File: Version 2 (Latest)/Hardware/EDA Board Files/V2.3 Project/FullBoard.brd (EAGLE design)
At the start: 281.5 x 99 mm, 187 parts, among them IC1 LM3914V, IC2 SGTL5000XNAA3, IC4 MCP73113-16SI_MF, IC5 NCP163ASN330T1G, J1 SJ-3524-SMT-TR, J10 SJ-3524-SMT-TR, J2 Teensy2, J3 Teensy1, J4 SJ-3524-SMT-TR, J7 1981584-1, J9 SJ-3524-SMT-TR, Q2 DMG9926USD-13, SW1 GATERON_LOW_PROFILE, SW10 GATERON_LOW_PROFILE, SW11 GATERON_LOW_PROFILE, SW12 GATERON_LOW_PROFILE, SW13 GATERON_LOW_PROFILE, SW14 GATERON_LOW_PROFILE, SW15 GATERON_LOW_PROFILE, SW16 GATERON_LOW_PROFILE, SW17 GATERON_LOW_PROFILE, SW18 GATERON_LOW_PROFILE, SW19 GATERON_LOW_PROFILE, SW2 GATERON_LOW_PROFILE, SW20 GATERON_LOW_PROFILE, SW21 GATERON_LOW_PROFILE, SW22 GATERON_LOW_PROFILE, SW23 GATERON_LOW_PROFILE, SW24 GATERON_LOW_PROFILE, SW25 GATERON_LOW_PROFILE, SW26 GATERON_LOW_PROFILE, SW27 GATERON_LOW_PROFILE, SW28 GATERON_LOW_PROFILE, SW29 GATERON_LOW_PROFILE, SW3 GATERON_LOW_PROFILE, SW30 GATERON_LOW_PROFILE, SW31 GATERON_LOW_PROFILE, SW32 GATERON_LOW_PROFILE, SW33 GATERON_LOW_PROFILE, SW34 GATERON_LOW_PROFILE, SW35 GATERON_LOW_PROFILE, SW36 GATERON_LOW_PROFILE, SW37 GATERON_LOW_PROFILE, SW38 GATERON_LOW_PROFILE, SW39 GATERON_LOW_PROFILE, SW4 GATERON_LOW_PROFILE, SW40 GATERON_LOW_PROFILE, SW41 GATERON_LOW_PROFILE, SW42 GATERON_LOW_PROFILE, SW43 GATERON_LOW_PROFILE, SW44 GATERON_LOW_PROFILE, SW45 GATERON_LOW_PROFILE, SW46 GATERON_LOW_PROFILE, SW47 GATERON_LOW_PROFILE, SW5 GATERON_LOW_PROFILE, SW6 GATERON_LOW_PROFILE, SW7 GATERON_LOW_PROFILE, SW8 GATERON_LOW_PROFILE, SW9 GATERON_LOW_PROFILE, U1 W25Q128FVSIG, U2 ATMEGA4809-AFR, U3 PAM2401, U4 MAX6775XKA+21-0076E_MXM-M, U5 AP7313-15SAG-7SOT-23_DIO-L, U6 S25FL512SAGMFIR13SO3016_SPA-M

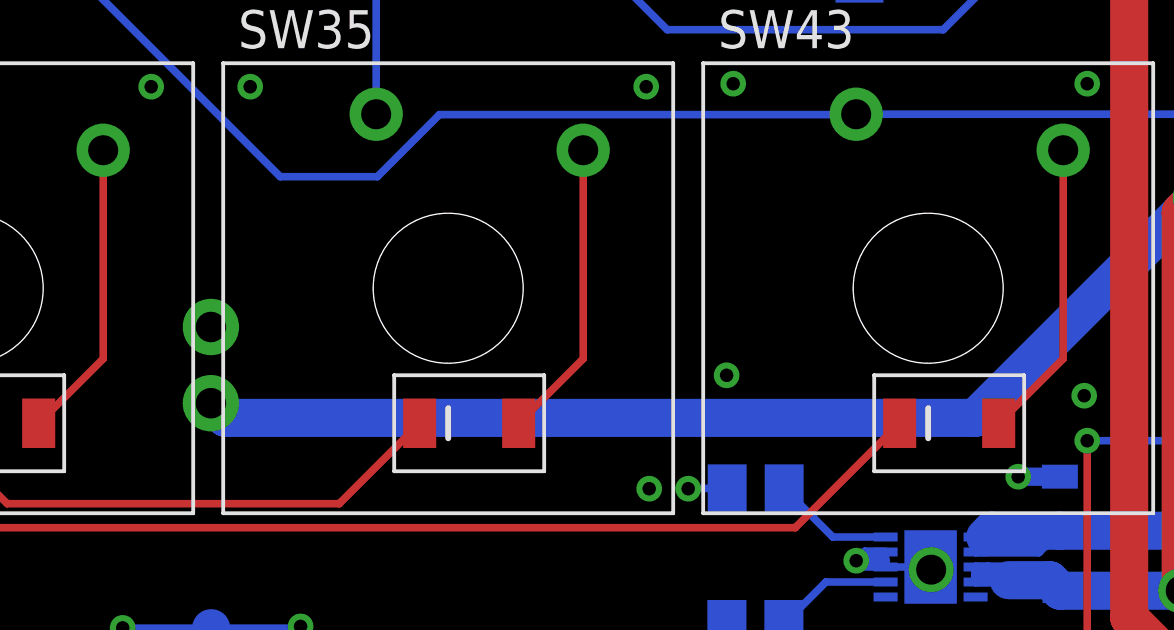
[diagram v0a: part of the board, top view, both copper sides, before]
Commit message: Updated battery connector on PCB
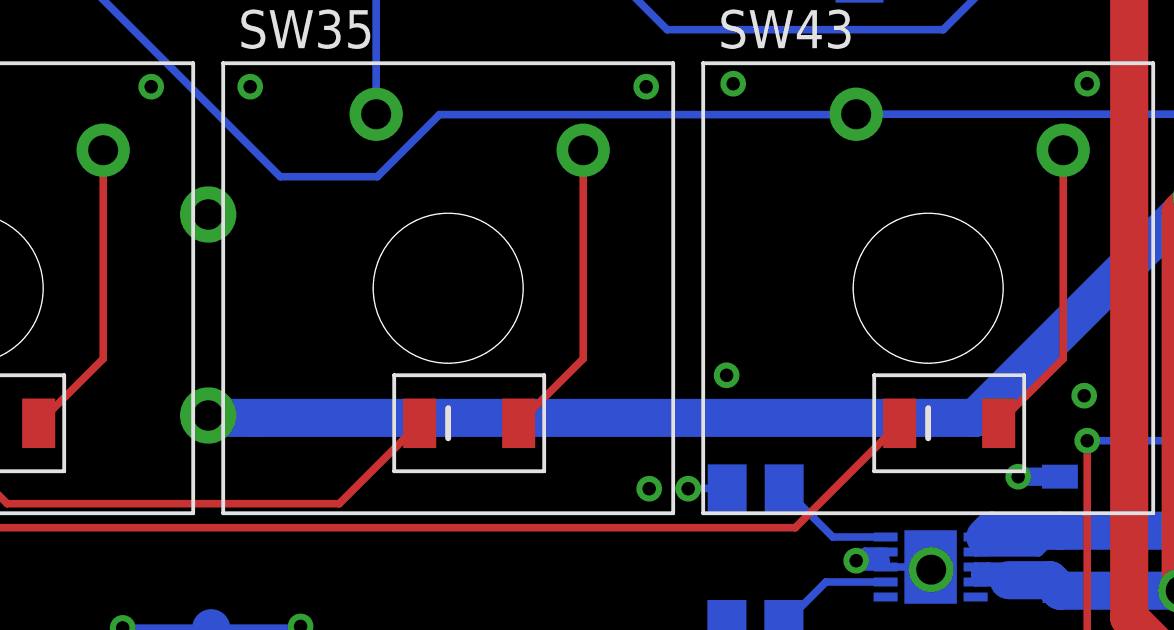
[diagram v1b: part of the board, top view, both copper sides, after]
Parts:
- removed J6: (no value), SparkFun-Connectors:1X02
- added J11, J12: (no value), SparkFun-Connectors:1X01
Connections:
- net GND: now also J12.1; no longer J6.2
- net LIPO+: now also J11.1; no longer J6.1
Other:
- board text added: "-"
- board text added: "Attach LiPo"
- board text added: "Here"
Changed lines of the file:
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@@
 <wire x1="3.59" y1="86.16" x2="3.59" y2="86.18" width="0.254" layer="26"/>
 <text x="168.01" y="46.07" size="1.4224" layer="26" rot="MR270">SI4703 Breakout</text>
+<text x="231.8" y="18.8" size="0.8128" layer="26" rot="MR0">Attach LiPo</text>
+<text x="230.2" y="17.8" size="0.8128" layer="26" rot="MR0">Here</text>
+<wire x1="229" y1="20.4" x2="229.6" y2="19.8" width="0.1524" layer="26"/>
+<wire x1="229" y1="20.4" x2="228.4" y2="19.8" width="0.1524" layer="26"/>
+<wire x1="229.6" y1="17.6" x2="229" y2="17" width="0.1524" layer="26"/>
+<wire x1="229" y1="17" x2="228.4" y2="17.6" width="0.1524" layer="26"/>
+<text x="229.7" y="12.2" size="1.778" layer="26" rot="MR0">+</text>
+<text x="229.54" y="23.39" size="2.1844" layer="26" rot="MR0">-</text>
 </plain>
 <attributes>
@@
 <attribute name="VALUE" x="270.83" y="73.21" size="1.27" layer="27" rot="R180" align="center"/>
 </element>
-<element name="J6" library="SparkFun-Connectors" package="1X02" value="" x="229.09" y="15.75" smashed="yes" rot="MR90">
-<attribute name="NAME" x="230.487" y="14.48" size="0.6096" layer="26" font="vector" ratio="20" rot="MR90"/>
-<attribute name="VALUE" x="227.058" y="14.48" size="0.6096" layer="28" font="vector" ratio="20" rot="MR90"/>
-</element>
 <element name="J7" library="audio amplifier example" library_urn="urn:adsk.eagle:library:970892" package="1981584-1" package3d_urn="urn:adsk.eagle:package:970926/2" value="1981584-1" x="281.03" y="9.68" smashed="yes" rot="MR270">
 <attribute name="MFPN" value="" x="434.7" y="-122.4" size="1.778" layer="28" rot="MR270" display="off"/>
@@
 <element name="TP3" library="SparkFun-Connectors" library_urn="urn:adsk.eagle:library:513" package="PAD.03X.05" package3d_urn="urn:adsk.eagle:package:38285/1" value="TEST-POINT3X5" x="273.23" y="46.23" smashed="yes" rot="MR0"/>
 <element name="TP4" library="SparkFun-Connectors" library_urn="urn:adsk.eagle:library:513" package="PAD.03X.05" package3d_urn="urn:adsk.eagle:package:38285/1" value="TEST-POINT3X5" x="229.1" y="8.25" smashed="yes" rot="MR0"/>
+<element name="J11" library="SparkFun-Connectors" library_urn="urn:adsk.eagle:library:513" package="1X01" package3d_urn="urn:adsk.eagle:package:38028/1" value="" x="229" y="15.34" smashed="yes" rot="MR0">
+<attribute name="VALUE" x="230.27" y="13.816" size="0.6096" layer="28" font="vector" ratio="20" rot="MR0" align="top-left"/>
+</element>
+<element name="J12" library="SparkFun-Connectors" library_urn="urn:adsk.eagle:library:513" package="1X01" package3d_urn="urn:adsk.eagle:package:38028/1" value="" x="229" y="22.04" smashed="yes" rot="MR0">
+<attribute name="VALUE" x="230.27" y="20.516" size="0.6096" layer="28" font="vector" ratio="20" rot="MR0" align="top-left"/>
+</element>
 </elements>
 <signals>
@@
 <contactref element="U4" pad="2"/>
 <contactref element="R23" pad="2"/>
-<contactref element="J6" pad="2"/>
 <contactref element="Q2" pad="3"/>
 <contactref element="R24" pad="2"/>
@@
 <wire x1="229.1" y1="8.25" x2="226.16" y2="8.25" width="0.254" layer="16"/>
 <wire x1="226.16" y1="8.25" x2="226.15" y2="8.26" width="0.254" layer="16"/>
+<contactref element="J12" pad="1"/>
 </signal>
 <signal name="SCL">
@@
 </signal>
 <signal name="LIPO+">
-<contactref element="J6" pad="1"/>
 <contactref element="U$1" pad="P$2"/>
 <contactref element="U$1" pad="P$5"/>
@@
 <wire x1="265.27" y1="23.75" x2="263.05" y2="23.75" width="1.27" layer="16"/>
 <wire x1="263.05" y1="23.75" x2="261.9" y2="22.6" width="1.27" layer="16"/>
-<wire x1="254.56" y1="15.26" x2="229.58" y2="15.26" width="1.27" layer="16"/>
-<wire x1="229.09" y1="15.75" x2="229.58" y2="15.26" width="1.27" layer="16"/>
+<wire x1="254.56" y1="15.26" x2="230.6" y2="15.26" width="1.27" layer="16"/>
+<wire x1="230.6" y1="15.26" x2="229.18" y2="15.26" width="1.27" layer="16"/>
 <wire x1="254.56" y1="15.26" x2="261.9" y2="22.6" width="1.27" layer="16"/>
 <wire x1="255.68335" y1="9.8502" x2="257.0498" y2="9.8502" width="1.27" layer="16"/>
@@
 <wire x1="271.067325" y1="23.723" x2="265.297" y2="23.723" width="1.21" layer="1"/>
 <wire x1="265.27" y1="23.75" x2="265.297" y2="23.723" width="1.21" layer="1"/>
+<contactref element="J11" pad="1"/>
+<wire x1="229.18" y1="15.26" x2="229.08" y2="15.26" width="1.27" layer="16"/>
+<wire x1="229.08" y1="15.26" x2="229" y2="15.34" width="1.27" layer="16"/>
 </signal>
 <signal name="CODEC_3.3V">
